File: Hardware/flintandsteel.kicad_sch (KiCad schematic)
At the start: 40 parts, among them J1 RBUS, U1 ESP32-S3, Y1 R940000171

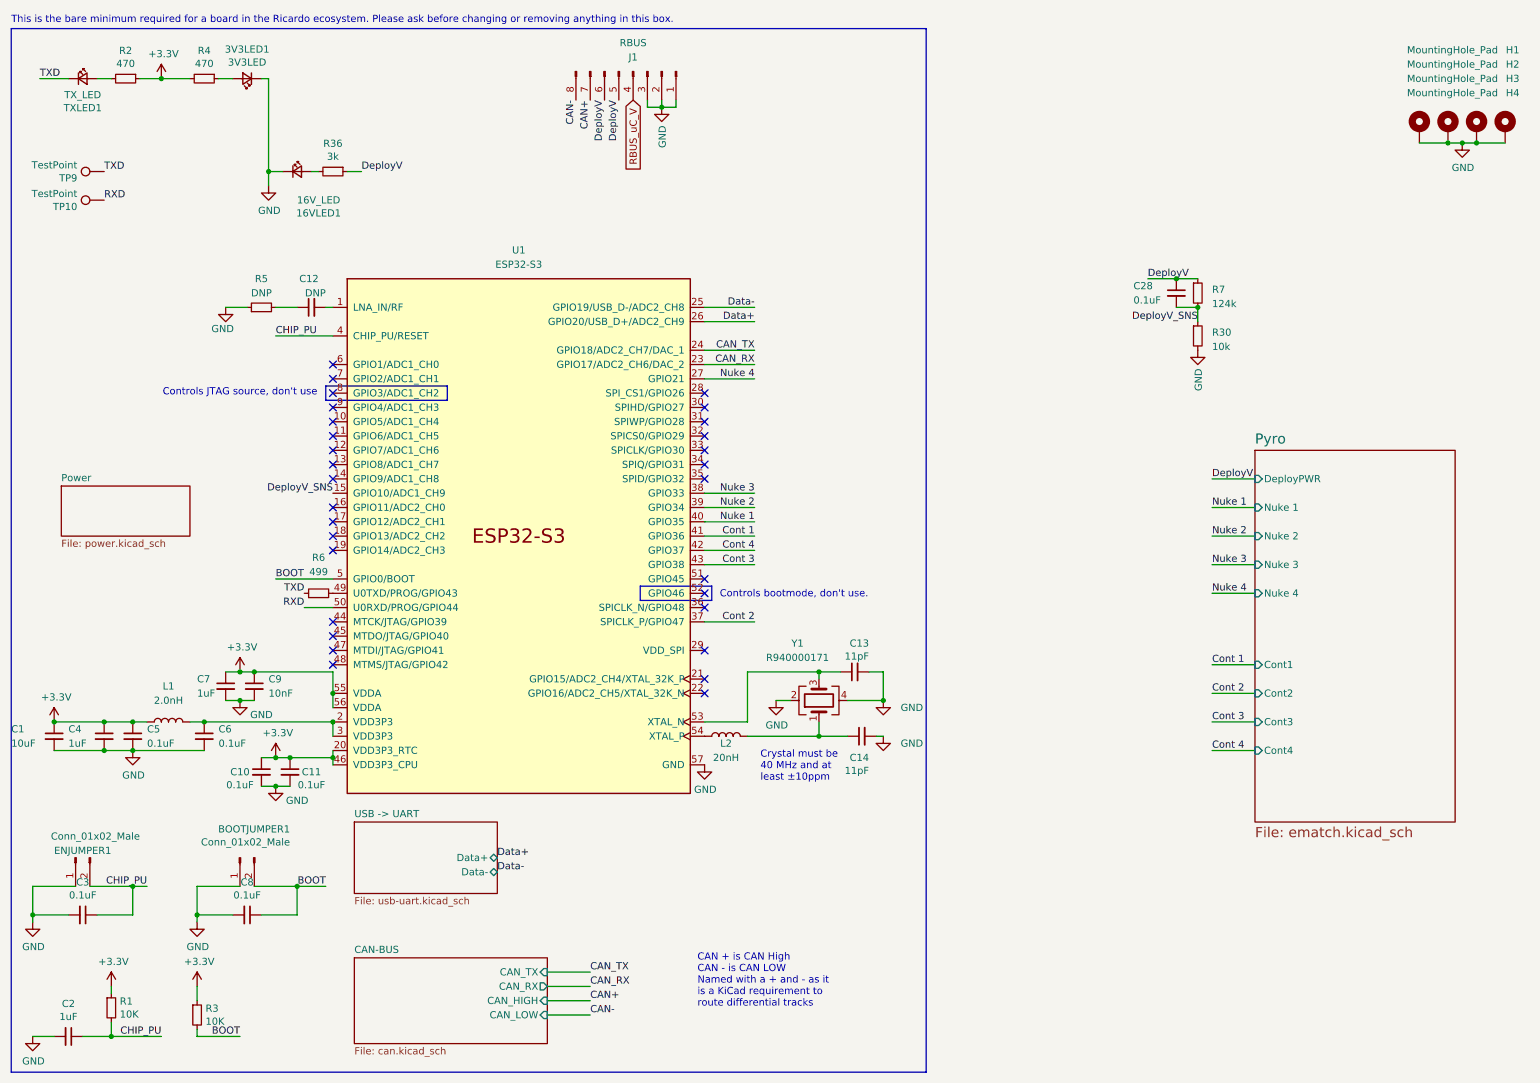
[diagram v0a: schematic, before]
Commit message: changed mosfets and added current sense circuit, layout not done
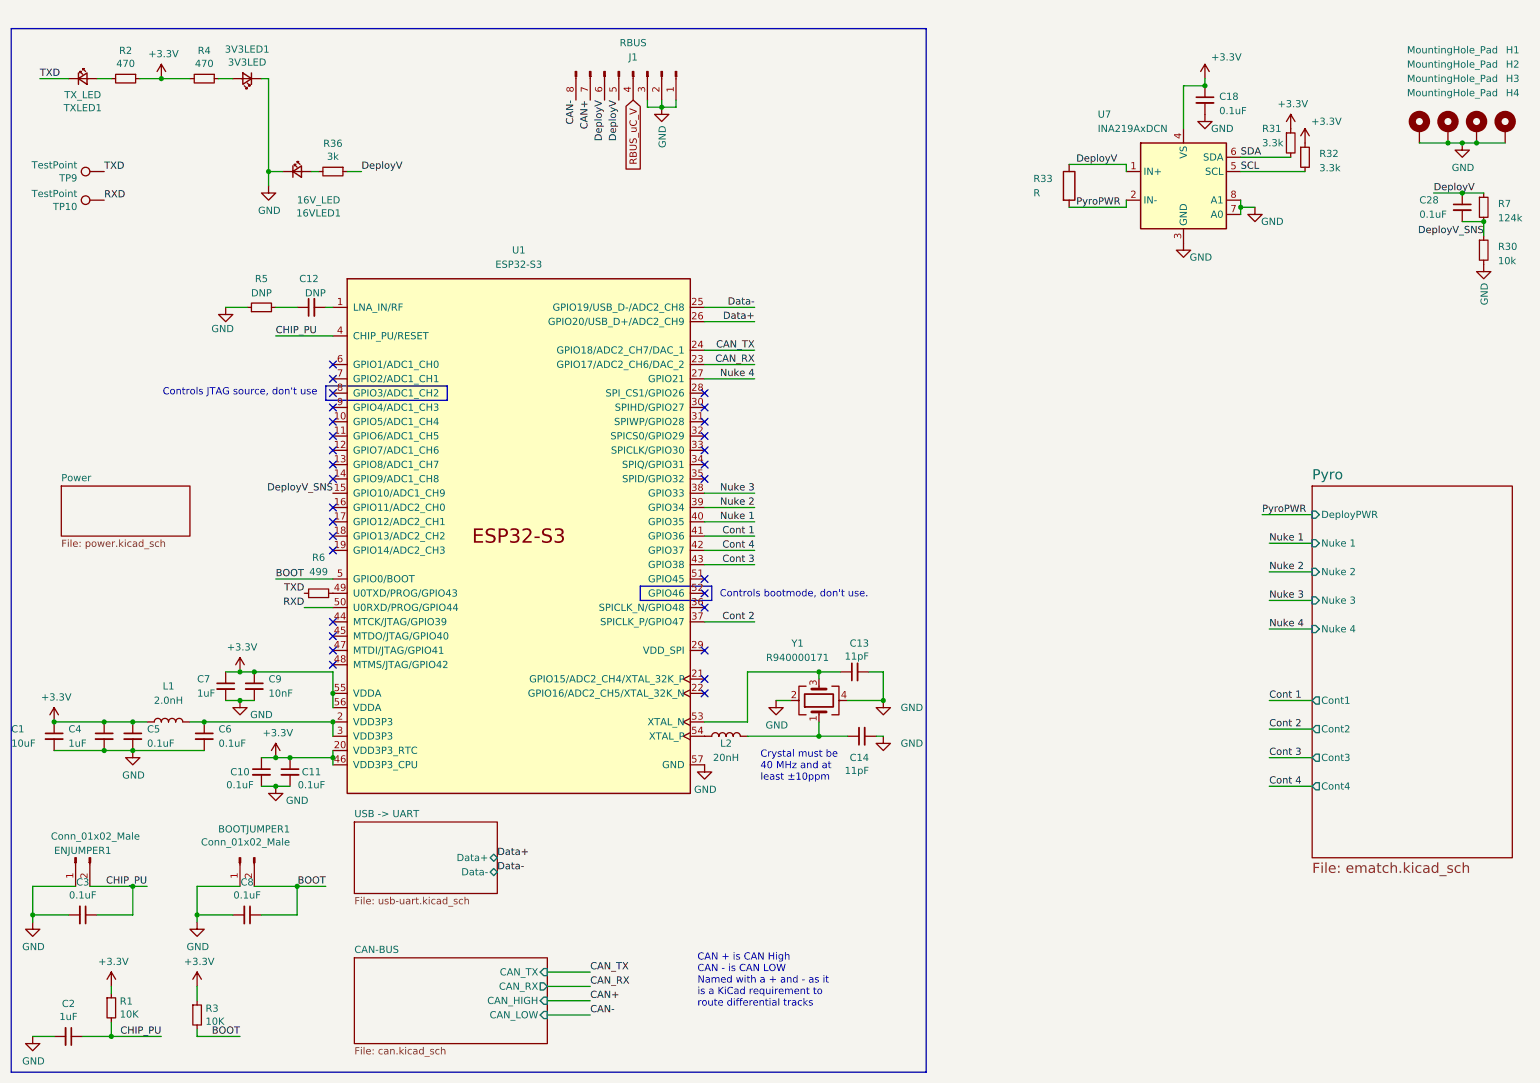
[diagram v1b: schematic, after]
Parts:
- added C18: 0.1uF, Capacitor_SMD:C_0402_1005Metric, symbol Device:C_Small
- added R31, R32: 3.3k, Resistor_SMD:R_0402_1005Metric, symbol Device:R_Small
- added R33: R, Resistor_SMD:R_0612_1632Metric, symbol Device:R
- added U7: INA219AxDCN, Package_TO_SOT_SMD:SOT-23-8, symbol Sensor_Energy:INA219AxDCN
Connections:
- net +3V3: now also C18.1, R31.1, R32.1, U7.4 (VS)
- net DeployV: now also R33.1, U7.1 (IN+)
- net GND: now also C18.2, U7.3 (GND), U7.7 (A0), U7.8 (A1)
- new net PyroPWR: R33.2, U7.2 (IN-)
- new net SCL: R32.2, U7.5 (SCL)
- new net SDA: R31.2, U7.6 (SDA)
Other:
- note removed: "This is the bare minimum required for a board in the Ricardo ecosystem. Please ask before changing or removing anything in this box."
- moved on the sheet: C28, R30, R7

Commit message: mostly finished new power layout, needs some vias and i2c routing
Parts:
- added C19: 0.1uF, Capacitor_SMD:C_0402_1005Metric, symbol Device:C_Small
- added R34, R35: 10, Resistor_SMD:R_0402_1005Metric, symbol Device:R_Small
- 16VLED1: value 16V_LED -> RED_LED
- 3V3LED1: value 3V3LED -> BLUE_LED
- R33: value R -> 2m; footprint Resistor_SMD:R_0612_1632Metric -> Resistor_SMD:R_2512_6332Metric_Pad1.40x3.35mm_HandSolder; Part Number (none) -> WSLF25122L000FEB
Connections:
- net SCL is gone; now on net SC+: R32.2, U7.5 (SCL)
- net SDA is gone; now on net SC-: R31.2, U7.6 (SDA)
- net DeployV: now also R34.1; no longer U7.1 (IN+)
- net PyroPWR: now also R35.1; no longer U7.2 (IN-)
- net SC-: now reaches U1.21 (GPIO15/ADC2_CH4/XTAL_32K_P)
- net SC+: now reaches U1.22 (GPIO16/ADC2_CH5/XTAL_32K_N)
- new net: C19.2, R35.2, U7.2 (IN-)
- new net: C19.1, R34.2, U7.1 (IN+)
- no-connect marks 30 -> 28
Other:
- moved on the sheet: R33
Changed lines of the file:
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@@
   (junction (at 59.69 142.24) (diameter 0) (color 0 0 0 0)
   )
+  (junction (at 203.2 36.83) (diameter 0) (color 0 0 0 0)
+  )
   (junction (at 53.34 127) (diameter 0) (color 0 0 0 0)
   )
@@
   )
   (junction (at 20.32 135.89) (diameter 0) (color 0 0 0 0)
+  )
+  (junction (at 203.2 44.45) (diameter 0) (color 0 0 0 0)
   )
   (junction (at 45.72 170.18) (diameter 0) (color 0 0 0 0)
@@
   (no_connect (at 69.85 123.19))
   (no_connect (at 135.89 92.71))
-  (no_connect (at 135.89 130.81))
   (no_connect (at 69.85 87.63))
   (no_connect (at 69.85 102.87))
@@
   (no_connect (at 135.89 82.55))
   (no_connect (at 69.85 125.73))
-  (no_connect (at 135.89 128.27))
   (wire (pts (xy 30.48 191.77) (xy 30.48 189.23))
     (stroke (width 0) (type default))
@@
     (stroke (width 0) (type default))
   )
+  (wire (pts (xy 203.2 36.83) (xy 203.2 38.1))
+    (stroke (width 0) (type default))
+  )
   (wire (pts (xy 29.21 135.89) (xy 34.29 135.89))
     (stroke (width 0) (type default))
@@
     (stroke (width 0) (type default))
   )
+  (wire (pts (xy 201.93 44.45) (xy 203.2 44.45))
+    (stroke (width 0) (type default))
+  )
   (wire (pts (xy 16.51 170.18) (xy 16.51 171.45))
     (stroke (width 0) (type default))
@@
     (stroke (width 0) (type default))
   )
+  (wire (pts (xy 201.93 36.83) (xy 203.2 36.83))
+    (stroke (width 0) (type default))
+  )
   (polyline (pts (xy 12.7 12.7) (xy 175.26 12.7))
     (stroke (width 0) (type default))
@@
     (stroke (width 0) (type default))
   )
-  (wire (pts (xy 200.66 44.45) (xy 210.82 44.45))
+  (wire (pts (xy 194.31 44.45) (xy 196.85 44.45))
     (stroke (width 0) (type default))
   )
@@
     (stroke (width 0) (type default))
   )
+  (wire (pts (xy 203.2 43.18) (xy 203.2 44.45))
+    (stroke (width 0) (type default))
+  )
   (polyline (pts (xy 137.16 114.3) (xy 124.46 114.3))
     (stroke (width 0) (type default))
   )
-  (wire (pts (xy 200.66 36.83) (xy 210.82 36.83))
+  (wire (pts (xy 194.31 36.83) (xy 196.85 36.83))
     (stroke (width 0) (type default))
   )
@@
     (stroke (width 0) (type default))
   )
+  (wire (pts (xy 203.2 36.83) (xy 210.82 36.83))
+    (stroke (width 0) (type default))
+  )
   (wire (pts (xy 74.93 38.1) (xy 72.39 38.1))
     (stroke (width 0) (type default))
@@
   )
   (wire (pts (xy 59.69 147.32) (xy 62.23 147.32))
+    (stroke (width 0) (type default))
+  )
+  (wire (pts (xy 203.2 44.45) (xy 210.82 44.45))
     (stroke (width 0) (type default))
   )
@@
     (effects (font (size 1.27 1.27)) (justify left bottom))
   )
-  (label "DeployV" (at 201.93 36.83 0) (fields_autoplaced)
-    (effects (font (size 1.27 1.27)) (justify left bottom))
-  )
   (label "DeployV" (at 118.11 25.4 270) (fields_autoplaced)
     (effects (font (size 1.27 1.27)) (justify right bottom))
@@
     (effects (font (size 1.27 1.27)) (justify right bottom))
   )
-  (label "SDA" (at 231.14 35.56 0) (fields_autoplaced)
+  (label "DeployV" (at 194.31 36.83 90) (fields_autoplaced)
+    (effects (font (size 1.27 1.27)) (justify left bottom))
+  )
+  (label "SC-" (at 231.14 35.56 0) (fields_autoplaced)
     (effects (font (size 1.27 1.27)) (justify left bottom))
   )
@@
     (effects (font (size 1.27 1.27)) (justify left bottom))
   )
+  (label "SC+" (at 135.89 130.81 0) (fields_autoplaced)
+    (effects (font (size 1.27 1.27)) (justify left bottom))
+  )
   (label "CAN_TX" (at 115.57 180.34 0) (fields_autoplaced)
     (effects (font (size 1.27 1.27)) (justify left bottom))
@@
     (effects (font (size 1.27 1.27)) (justify right bottom))
   )
-  (label "PyroPWR" (at 201.93 44.45 0) (fields_autoplaced)
-    (effects (font (size 1.27 1.27)) (justify left bottom))
-  )
-  (label "SCL" (at 231.14 38.1 0) (fields_autoplaced)
+  (label "SC+" (at 231.14 38.1 0) (fields_autoplaced)
     (effects (font (size 1.27 1.27)) (justify left bottom))
   )
@@
     (effects (font (size 1.27 1.27)) (justify left bottom))
   )
+  (label "SC-" (at 135.89 128.27 0) (fields_autoplaced)
+    (effects (font (size 1.27 1.27)) (justify left bottom))
+  )
   (label "CHIP_PU" (at 59.69 67.31 0) (fields_autoplaced)
     (effects (font (size 1.27 1.27)) (justify left bottom))
@@
   (label "TXD" (at 17.78 21.59 0) (fields_autoplaced)
     (effects (font (size 1.27 1.27)) (justify left bottom))
+  )
+  (label "PyroPWR" (at 194.31 44.45 270) (fields_autoplaced)
+    (effects (font (size 1.27 1.27)) (justify right bottom))
   )
   (label "CHIP_PU" (at 39.37 191.77 180) (fields_autoplaced)
@@
       (effects (font (size 1.27 1.27)))
     )
-    (property "Value" "3V3LED" (at 54.61 18.6944 0)
+    (property "Value" "BLUE_LED" (at 54.61 18.6944 0)
       (effects (font (size 1.27 1.27)))
     )
@@
   (symbol (lib_id "Device:LED_Small") (at 63.5 38.1 0) (unit 1)
     (in_bom yes) (on_board yes) (dnp no)
-    (property "Reference" "16VLED1" (at 67.31 45.4914 0)
-      (effects (font (size 1.27 1.27)))
-    )
-    (property "Value" "16V_LED" (at 67.31 43.18 0)
+    (property "Reference" "16VLED1" (at 69.85 41.91 0)
+      (effects (font (size 1.27 1.27)))
+    )
+    (property "Value" "RED_LED" (at 69.85 44.2214 0)
       (effects (font (size 1.27 1.27)))
     )
@@
     )
   )
-  (symbol (lib_id "Device:R") (at 200.66 40.64 0) (unit 1)
-    (in_bom yes) (on_board yes) (dnp no)
-    (property "Reference" "R33" (at 194.31 39.37 0)
-      (effects (font (size 1.27 1.27)) (justify left))
-    )
-    (property "Value" "R" (at 194.31 41.91 0)
-      (effects (font (size 1.27 1.27)) (justify left))
-    )
-    (property "Footprint" "Resistor_SMD:R_0612_1632Metric" (at 198.882 40.64 90)
-      (effects (font (size 1.27 1.27)) hide)
-    )
-    (property "Datasheet" "~" (at 200.66 40.64 0)
-      (effects (font (size 1.27 1.27)) hide)
+  (symbol (lib_id "Device:R") (at 194.31 40.64 0) (unit 1)
+    (in_bom yes) (on_board yes) (dnp no)
+    (property "Reference" "R33" (at 187.96 39.37 0)
+      (effects (font (size 1.27 1.27)) (justify left))
+    )
+    (property "Value" "2m" (at 189.23 41.91 0)
+      (effects (font (size 1.27 1.27)) (justify left))
+    )
+    (property "Footprint" "Resistor_SMD:R_2512_6332Metric_Pad1.40x3.35mm_HandSolder" (at 192.532 40.64 90)
+      (effects (font (size 1.27 1.27)) hide)
+    )
+    (property "Datasheet" "~" (at 194.31 40.64 0)
+      (effects (font (size 1.27 1.27)) hide)
+    )
+    (property "Part Number" "WSLF25122L000FEB" (at 186.69 40.64 90)
+      (effects (font (size 1.27 1.27)))
     )
     (pin "1")
@@
     )
   )
+  (symbol (lib_id "Device:R_Small") (at 199.39 44.45 90) (unit 1)
+    (in_bom yes) (on_board yes) (dnp no) (fields_autoplaced)
+    (property "Reference" "R35" (at 199.39 39.37 90)
+      (effects (font (size 1.27 1.27)))
+    )
+    (property "Value" "10" (at 199.39 41.91 90)
+      (effects (font (size 1.27 1.27)))
+    )
+    (property "Footprint" "Resistor_SMD:R_0402_1005Metric" (at 199.39 44.45 0)
+      (effects (font (size 1.27 1.27)) hide)
+    )
+    (property "Datasheet" "~" (at 199.39 44.45 0)
+      (effects (font (size 1.27 1.27)) hide)
+    )
+    (pin "1")
+    (pin "2")
+    (instances
+      (project "flintandsteel"
+        (path "/7db990e4-92e1-4f99-b4d2-435bbec1ba83"
+          (reference "R35") (unit 1)
+        )
+      )
+    )
+  )
   (symbol (lib_id "Device:C_Small") (at 62.23 144.78 0) (unit 1)
     (in_bom yes) (on_board yes) (dnp no)
@@
         (path "/7db990e4-92e1-4f99-b4d2-435bbec1ba83"
           (reference "#PWR020") (unit 1)
+        )
+      )
+    )
+  )
+  (symbol (lib_id "Device:R_Small") (at 199.39 36.83 90) (unit 1)
+    (in_bom yes) (on_board yes) (dnp no) (fields_autoplaced)
+    (property "Reference" "R34" (at 199.39 31.75 90)
+      (effects (font (size 1.27 1.27)))
+    )
+    (property "Value" "10" (at 199.39 34.29 90)
+      (effects (font (size 1.27 1.27)))
+    )
+    (property "Footprint" "Resistor_SMD:R_0402_1005Metric" (at 199.39 36.83 0)
+      (effects (font (size 1.27 1.27)) hide)
+    )
+    (property "Datasheet" "~" (at 199.39 36.83 0)
+      (effects (font (size 1.27 1.27)) hide)
+    )
+    (pin "1")
+    (pin "2")
+    (instances
+      (project "flintandsteel"
+        (path "/7db990e4-92e1-4f99-b4d2-435bbec1ba83"
+          (reference "R34") (unit 1)
         )
       )
@@
         )
       )
+    )
+  )
+  (symbol (lib_id "Device:C_Small") (at 203.2 40.64 0) (unit 1)
+    (in_bom yes) (on_board yes) (dnp no) (fields_autoplaced)
+    (property "Reference" "C19" (at 205.74 40.0113 0)
+      (effects (font (size 1.27 1.27)) (justify left))
+    )
+    (property "Value" "0.1uF" (at 205.74 42.5513 0)
+      (effects (font (size 1.27 1.27)) (justify left))
+    )
+    (property "Footprint" "Capacitor_SMD:C_0402_1005Metric" (at 203.2 40.64 0)
+      (effects (font (size 1.27 1.27)) hide)
+    )
+    (property "Datasheet" "~" (at 203.2 40.64 0)
+      (effects (font (size 1.27 1.27)) hide)
+    )
+    (pin "1")
+    (pin "2")
+    (instances
+      (project "flintandsteel"
+        (path "/7db990e4-92e1-4f99-b4d2-435bbec1ba83"
+          (reference "C19") (unit 1)
+        )
+      )

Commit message: v2.1
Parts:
- 16VLED1, 3V3LED1, TXLED1: footprint Diode_SMD:D_0402_1005Metric -> LED_SMD:LED_0402_1005Metric
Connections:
- net DeployV_SNS: no longer U1.15 (GPIO10/ADC1_CH9)
- net SCL: now reaches U1.16 (GPIO11/ADC2_CH0)
- net SCL: now also R32.2, U7.5 (SCL)
- removed net SC+: R32.2, U1.22 (GPIO16/ADC2_CH5/XTAL_32K_N), U7.5 (SCL)
- net SC- renamed SDA
- net SDA: now also U1.15 (GPIO10/ADC1_CH9); no longer U1.21 (GPIO15/ADC2_CH4/XTAL_32K_P)
- no-connect marks 28 -> 29
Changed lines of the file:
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@@
   )
   (no_connect (at 69.85 100.33))
-  (no_connect (at 69.85 97.79))
   (no_connect (at 69.85 123.19))
   (no_connect (at 135.89 92.71))
@@
   (no_connect (at 135.89 115.57))
   (no_connect (at 69.85 90.17))
+  (no_connect (at 135.89 130.81))
   (no_connect (at 69.85 72.39))
   (no_connect (at 135.89 87.63))
   (no_connect (at 135.89 80.01))
   (no_connect (at 69.85 92.71))
+  (no_connect (at 135.89 128.27))
   (no_connect (at 69.85 77.47))
   (no_connect (at 69.85 82.55))
@@
     (effects (font (size 1.27 1.27)) (justify left bottom))
   )
+  (label "SCL" (at 69.85 97.79 180) (fields_autoplaced)
+    (effects (font (size 1.27 1.27)) (justify right bottom))
+  )
   (label "DeployV" (at 118.11 25.4 270) (fields_autoplaced)
     (effects (font (size 1.27 1.27)) (justify right bottom))
@@
     (effects (font (size 1.27 1.27)) (justify left bottom))
   )
-  (label "SC-" (at 231.14 35.56 0) (fields_autoplaced)
+  (label "SDA" (at 231.14 35.56 0) (fields_autoplaced)
     (effects (font (size 1.27 1.27)) (justify left bottom))
   )
@@
     (effects (font (size 1.27 1.27)) (justify right bottom))
   )
+  (label "SDA" (at 69.85 95.25 180) (fields_autoplaced)
+    (effects (font (size 1.27 1.27)) (justify right bottom))
+  )
   (label "DeployV" (at 74.93 38.1 0) (fields_autoplaced)
     (effects (font (size 1.27 1.27)) (justify left bottom))
@@
     (effects (font (size 1.27 1.27)) (justify left bottom))
   )
-  (label "SC+" (at 135.89 130.81 0) (fields_autoplaced)
-    (effects (font (size 1.27 1.27)) (justify left bottom))
-  )
   (label "CAN_TX" (at 115.57 180.34 0) (fields_autoplaced)
     (effects (font (size 1.27 1.27)) (justify left bottom))
@@
     (effects (font (size 1.27 1.27)) (justify right bottom))
   )
-  (label "SC+" (at 231.14 38.1 0) (fields_autoplaced)
+  (label "SCL" (at 231.14 38.1 0) (fields_autoplaced)
     (effects (font (size 1.27 1.27)) (justify left bottom))
   )
@@
     (effects (font (size 1.27 1.27)) (justify left bottom))
   )
-  (label "SC-" (at 135.89 128.27 0) (fields_autoplaced)
-    (effects (font (size 1.27 1.27)) (justify left bottom))
-  )
   (label "CHIP_PU" (at 59.69 67.31 0) (fields_autoplaced)
     (effects (font (size 1.27 1.27)) (justify left bottom))
@@
   )
   (label "Cont 3" (at 144.78 107.95 180) (fields_autoplaced)
-    (effects (font (size 1.27 1.27)) (justify right bottom))
-  )
-  (label "DeployV_SNS" (at 69.85 95.25 180) (fields_autoplaced)
     (effects (font (size 1.27 1.27)) (justify right bottom))
   )
@@
       (effects (font (size 1.27 1.27)))
     )
-    (property "Footprint" "Diode_SMD:D_0402_1005Metric" (at 25.4 21.59 90)
+    (property "Footprint" "LED_SMD:LED_0402_1005Metric" (at 25.4 21.59 90)
       (effects (font (size 1.27 1.27)) hide)
     )
@@
       (effects (font (size 1.27 1.27)))
     )
-    (property "Footprint" "Diode_SMD:D_0402_1005Metric" (at 54.61 21.59 90)
+    (property "Footprint" "LED_SMD:LED_0402_1005Metric" (at 54.61 21.59 90)
       (effects (font (size 1.27 1.27)) hide)
     )
@@
       (effects (font (size 1.27 1.27)))
     )
-    (property "Footprint" "Diode_SMD:D_0402_1005Metric" (at 63.5 38.1 90)
-      (effects (font (size 1.27 1.27)) hide)
-    )
+    (property "Footprint" "LED_SMD:LED_0402_1005Metric" (at 63.5 38.1 90)
+      (effects (font (size 1.27 1.27)) hide)
+    )
